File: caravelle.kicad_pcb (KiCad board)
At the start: 2 copper layers, 277.4 x 94.1 mm, 71 parts, among them J1 Conn_01x04, J2 Conn_01x02_Female, J3 Conn_01x04, J4 Conn_01x02_Female, J5 Conn_01x01, J6 Conn_01x01, K1 keyboard_parts_KEYSW, K10 keyboard_parts_KEYSW, K11 keyboard_parts_KEYSW, K12 keyboard_parts_KEYSW, K13 keyboard_parts_KEYSW, K14 keyboard_parts_KEYSW, K15 keyboard_parts_KEYSW, K16 keyboard_parts_KEYSW, K17 keyboard_parts_KEYSW, K18 keyboard_parts_KEYSW, K19 keyboard_parts_KEYSW, K2 keyboard_parts_KEYSW, K20 keyboard_parts_KEYSW, K21 keyboard_parts_KEYSW, K22 keyboard_parts_KEYSW, K23 keyboard_parts_KEYSW, K24 keyboard_parts_KEYSW, K25 keyboard_parts_KEYSW, K26 keyboard_parts_KEYSW, K27 keyboard_parts_KEYSW, K28 keyboard_parts_KEYSW, K29 keyboard_parts_KEYSW, K3 keyboard_parts_KEYSW, K30 keyboard_parts_KEYSW, K31 keyboard_parts_KEYSW, K32 keyboard_parts_KEYSW, K33 keyboard_parts_KEYSW, K34 keyboard_parts_KEYSW, K35 keyboard_parts_KEYSW, K36 keyboard_parts_KEYSW, K37 keyboard_parts_KEYSW, K38 keyboard_parts_KEYSW, K39 keyboard_parts_KEYSW, K4 keyboard_parts_KEYSW, K40 keyboard_parts_KEYSW, K41 keyboard_parts_KEYSW, K42 keyboard_parts_KEYSW, K43 keyboard_parts_KEYSW, K44 keyboard_parts_KEYSW, K45 keyboard_parts_KEYSW, K46 keyboard_parts_KEYSW, K47 keyboard_parts_KEYSW, K48 keyboard_parts_KEYSW, K5 keyboard_parts_KEYSW, K6 keyboard_parts_KEYSW, K7 keyboard_parts_KEYSW, K8 keyboard_parts_KEYSW, K9 keyboard_parts_KEYSW, SW1 SW_SPDT, SW2 SW_SPDT, SW3 RESET_SW, SW4 RESET_SW, U1 BL652_LEFT, U11 logo1, U12 logo2, U13 logo1, U2 hole, U3 hole, U4 hole, U5 BL652_RIGHT, U6 hole, U7 hole, U8 hole

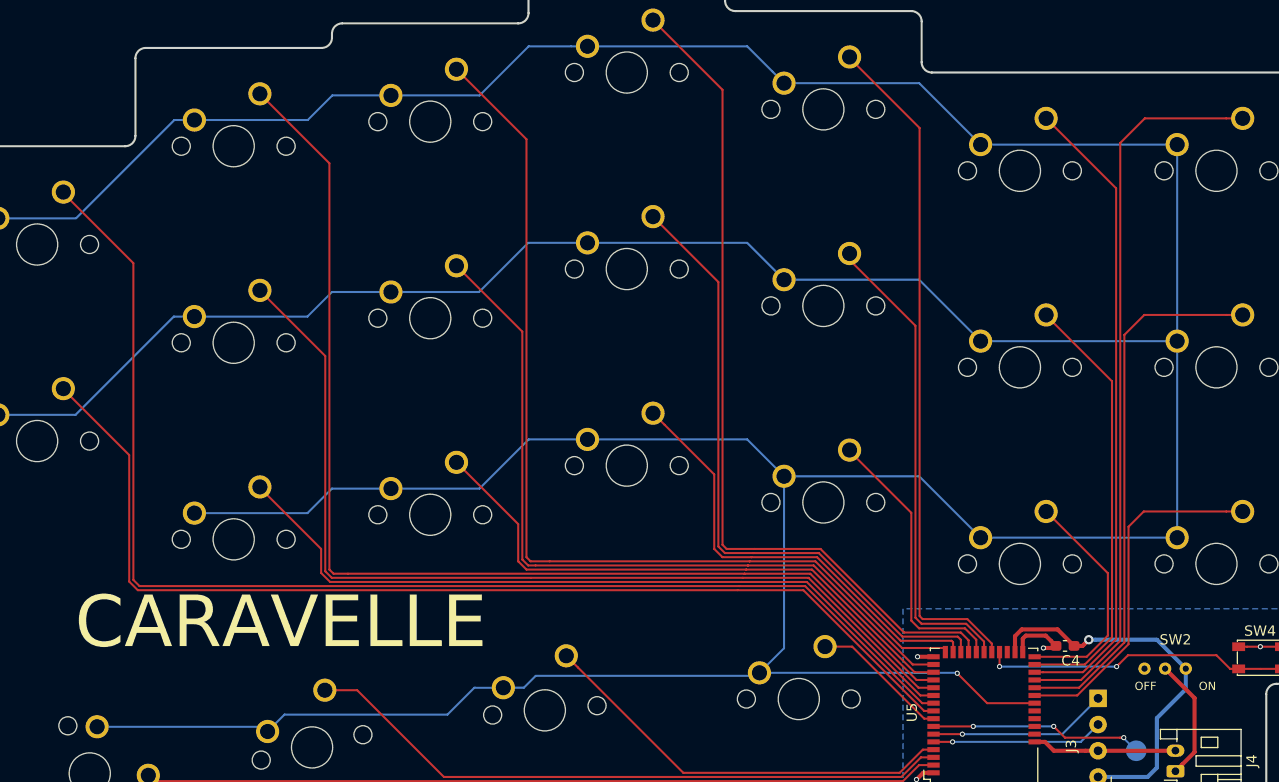
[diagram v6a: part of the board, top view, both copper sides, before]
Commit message: Change matrix wiring
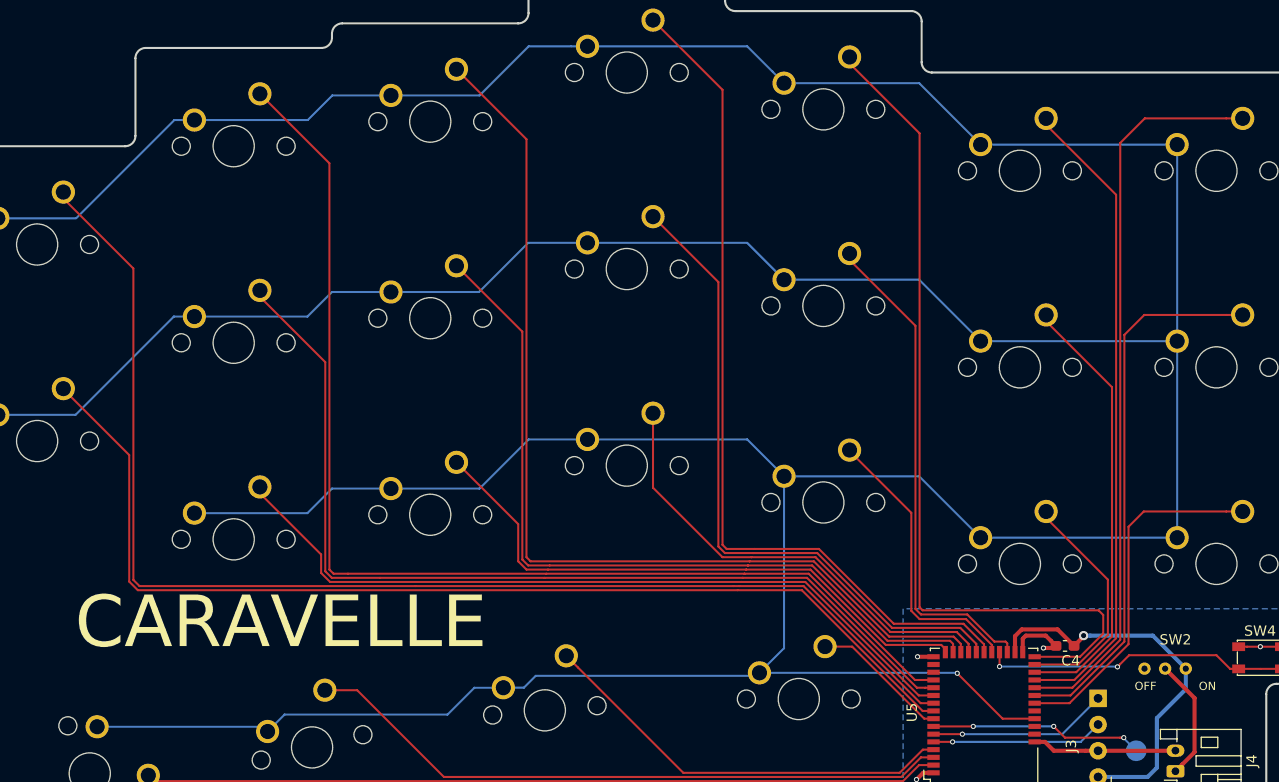
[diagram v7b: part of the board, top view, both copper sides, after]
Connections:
- U5 pad 14: /R18 -> Net-(U5-Pad14)
- U5 pad 15: /R11 -> Net-(U5-Pad15)
- U5 pad 17: /R5 -> /R18
- U5 pad 18: /R17 -> /R11
- U5 pad 19: /R10 -> /R5
- U5 pad 20: /R4 -> /R17
- U5 pad 21: /R16 -> /R10
- U5 pad 22: /R9 -> /R4
- U5 pad 23: /R3 -> /R16
- U5 pad 25: Net-(U5-Pad25) -> /R9
- U5 pad 28: /R15 -> /R3
- U5 pad 29: /R8 -> /R15
- U5 pad 30: /R2 -> /R8
- U5 pad 31: /R1 -> /R2
- U5 pad 32: /R7 -> /R1
- U5 pad 33: /R14 -> /R7
- U5 pad 34: /ROW_R -> /R14
- U5 pad 36: Net-(U5-Pad36) -> /ROW_R
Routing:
- net /R3: track 65.7 -> 83.1 mm
- net /R5: track 94.1 -> 96.5 mm
- net /R11: track 75.2 -> 77.1 mm
- net /R9: track 46.0 -> 47.7 mm
- net /R17: track 43.5 -> 44.9 mm
- net /R4: track 82.3 -> 83.5 mm
- net /R10: track 63.0 -> 64.3 mm
- net /R16: track 27.3 -> 27.9 mm
- net /ROW_R: track 505.2 -> 505.8 mm

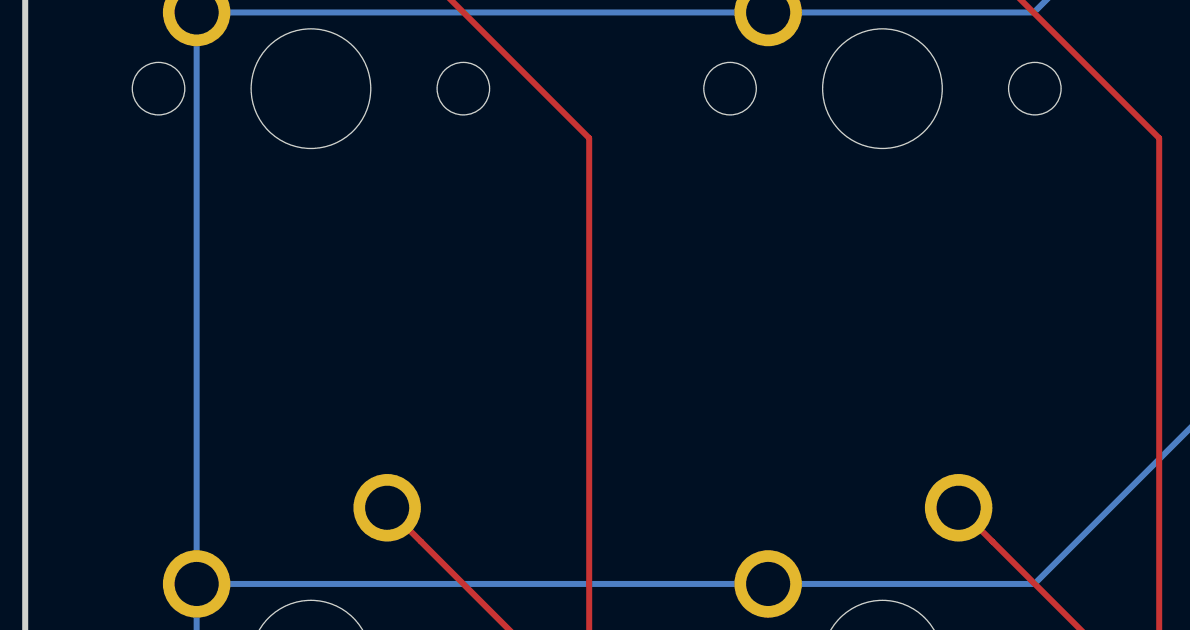
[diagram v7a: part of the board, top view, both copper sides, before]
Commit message: Change logo from silk to mask
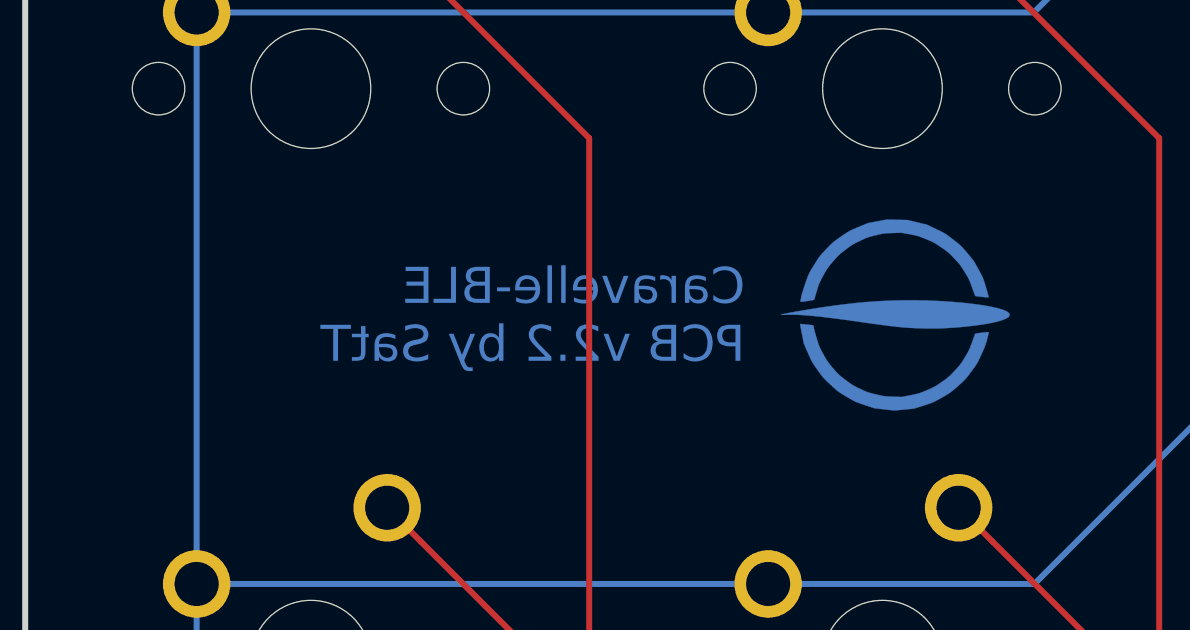
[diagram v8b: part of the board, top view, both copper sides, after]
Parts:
- moved U12 1.40 mm to (79.0, 76.6)
